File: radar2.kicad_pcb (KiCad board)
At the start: 4 copper layers, 127 parts, among them IC1 BQ25713RSNR, IC2 TPS54540DDA, IC3 LP5907QMFX-3.0Q1, IC5 LP5907QMFX-3.0Q1, IC6 DW3220TR13, J1 GSB1C4621DS1HR, J2 M20-8770546 (for SWD), J3 M20-9730446_DISPLAY_POWER, J4 JST-XH, J5 M20-9990646_PI, J6 SMA_CONNECTOR, J7 SMA_CONNECTOR, Q1 CSD17308Q3, Q2 CSD17308Q3, Q3 CSD17308Q3, Q4 CSD17308Q3, Q5 CSD25404Q3, SW1 09.03290.01, SW2 SWT0220-016016GSA, U1 STM32H725ZETx, Y1 ECS-384-CDX-2482

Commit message: starting routing
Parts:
- moved SW1 94.0 mm to (113.6, 111.5), turned to 90 degrees
- moved J2 68.2 mm to (121.2, 65.6), turned to -90 degrees
- moved J4 26.9 mm to (169.3, 112.8)
- moved C1 22.0 mm to (155.5, 102.5)
- moved C13 22.0 mm to (117.8, 89.0)
- moved C14 22.0 mm to (122.0, 89.0)
- moved C16 22.0 mm to (115.8, 89.0)
- moved C19 22.0 mm to (133.9, 96.9)
- moved C20 22.0 mm to (137.8, 95.8)
- moved C21 22.0 mm to (142.4, 90.9)
- moved C25 22.0 mm to (182.4, 88.4)
- moved C26 22.0 mm to (179.9, 88.4)
- moved C28 22.0 mm to (174.9, 88.4)
- moved C29 22.0 mm to (172.4, 88.4)
- moved C3 22.0 mm to (160.4, 93.8)
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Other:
- board outline added: 127.2 x 59.1 mm

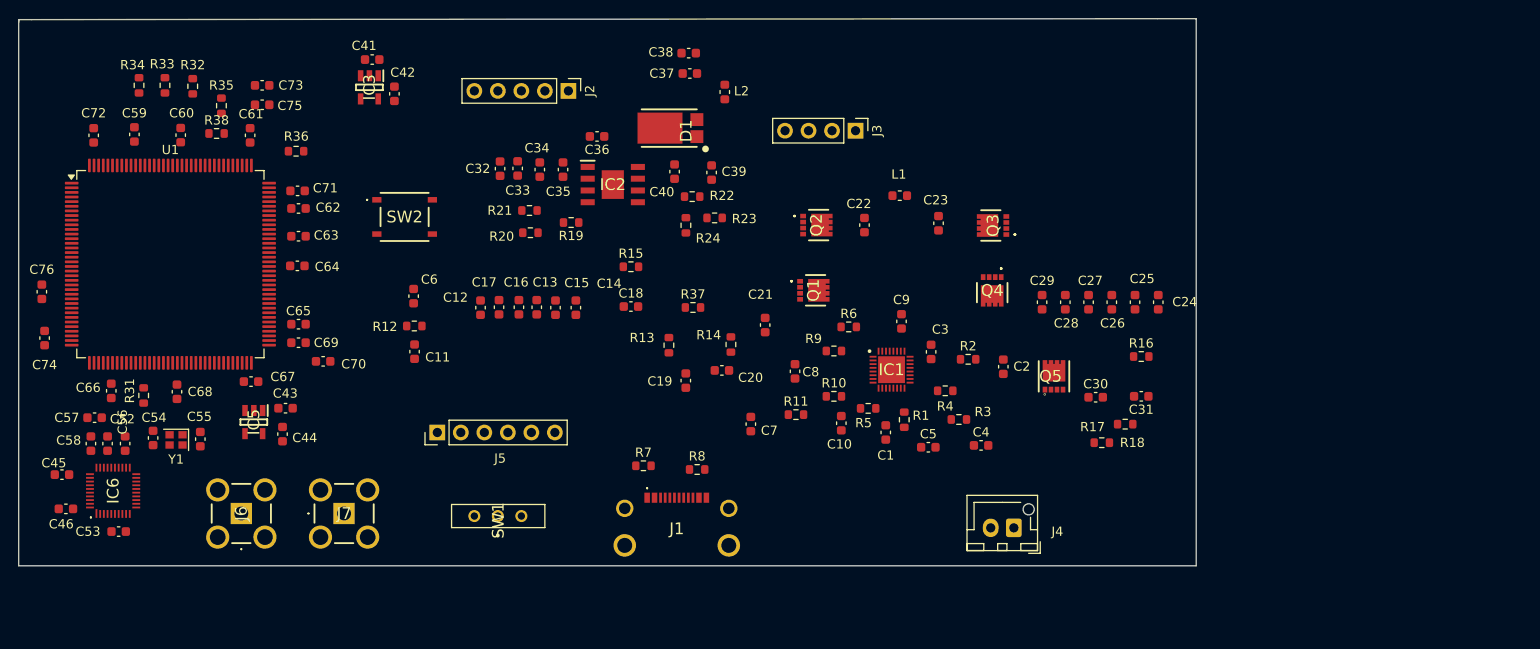
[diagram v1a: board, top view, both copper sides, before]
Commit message: routing on rf ic DW3220
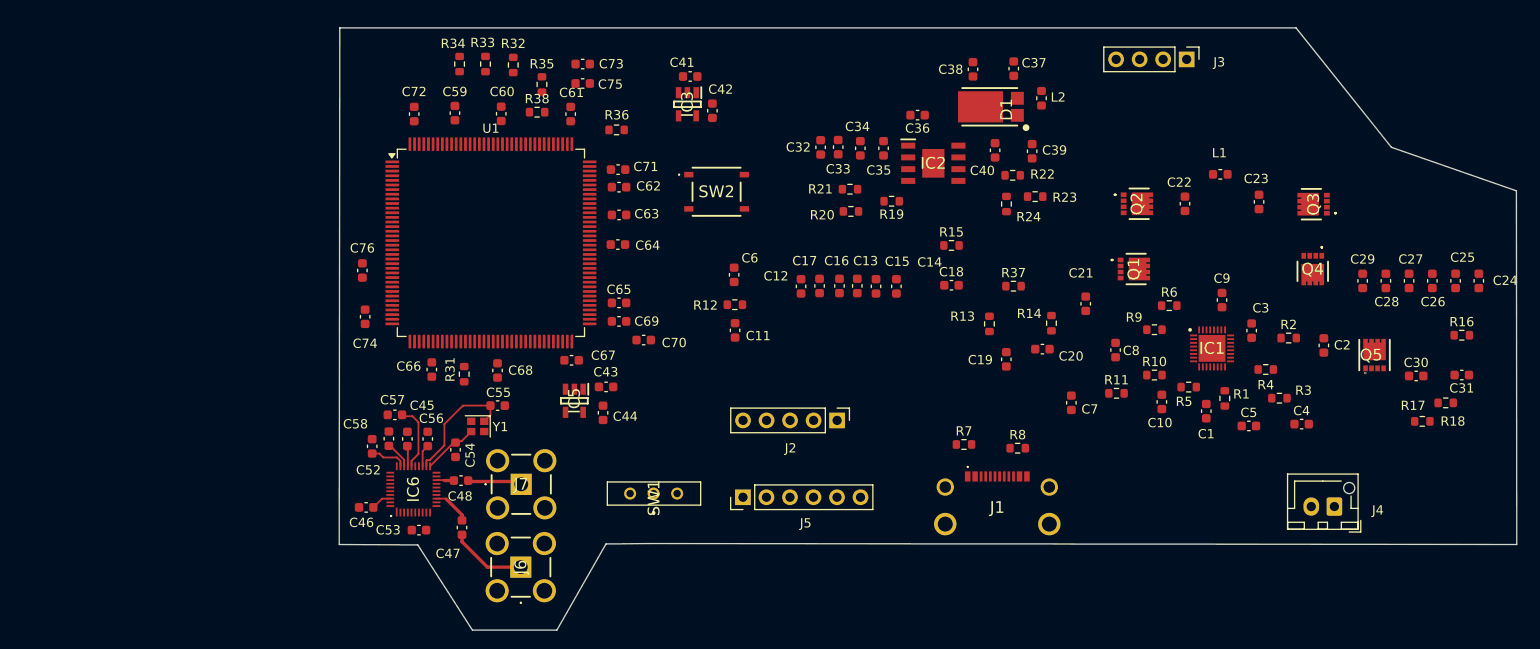
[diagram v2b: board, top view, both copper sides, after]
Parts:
- added C47: 2.0pF, Capacitor_SMD:C_0603_1608Metric, F.Cu at (109.7, 112.8)
- added C48: 2.0pF, Capacitor_SMD:C_0603_1608Metric, F.Cu at (109.6, 107.7)
- moved J2 45.9 mm to (150.2, 101.2)
- moved C45 37.5 mm to (103.8, 103.2), turned to -90 degrees
- moved J3 36.6 mm to (188.0, 62.2)
- moved C37 35.0 mm to (169.3, 63.2), turned to -90 degrees
- moved C15 34.7 mm to (154.4, 86.7)
- moved C34 34.7 mm to (152.7, 71.8)
- moved C36 34.7 mm to (158.9, 68.2)
- moved R12 34.7 mm to (139.2, 88.7)
- moved C1 34.7 mm to (190.1, 100.2)
- moved C10 34.7 mm to (185.3, 99.2)
- moved C13 34.7 mm to (152.4, 86.7)
- moved C14 34.7 mm to (156.6, 86.7)
- moved C16 34.7 mm to (150.5, 86.7)
- moved C19 34.7 mm to (168.5, 94.6)
- moved C2 34.7 mm to (202.8, 93.1)
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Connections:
- J6 pad 1: GND -> Net-(C47-Pad2)
- J6 pad 5: DW_RF2 -> GND
- J7 pad 1: GND -> Net-(C48-Pad2)
- J7 pad 5: DW_RF1 -> GND
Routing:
- net 3V3_RADAR: track 0.00 -> 16.3 mm
- net DW_XTO: track 0.00 -> 13.3 mm
- net Net-(C47-Pad2): track 0.00 -> 8.24 mm
- net DW_XTI: track 0.00 -> 6.00 mm
- net Net-(C48-Pad2): track 0.00 -> 5.89 mm
- net DW_RF2: track 0.00 -> 4.07 mm
- net GND: track 0.00 -> 3.03 mm
- net Net-(IC6-VIO_D): track 0.00 -> 2.22 mm
- net Net-(IC6-VTX_D): track 0.00 -> 2.05 mm
- net DW_RF1: track 0.00 -> 1.90 mm
- added copper zone on In1.Cu, net GND
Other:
- board size 127.2 x 59.1 mm -> 127.2 x 65 mm

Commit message: changing sizes of caps from 06 to 04, also using vias on DW spi interfact to stm32
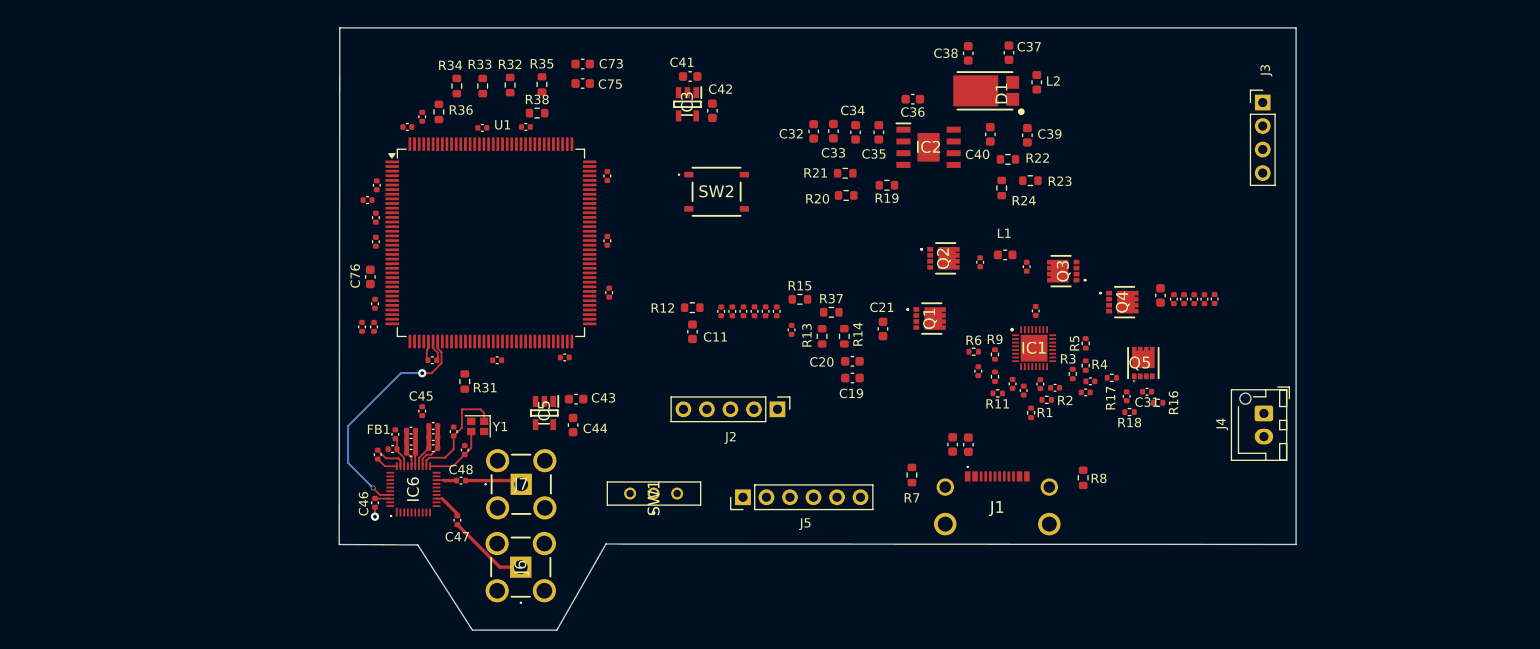
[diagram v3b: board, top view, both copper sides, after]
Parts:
- added C49: 0.1uF, Capacitor_SMD:C_0402_1005Metric, F.Cu at (106.6, 104.2)
- added C50: 4.7nF, Capacitor_SMD:C_0402_1005Metric, F.Cu at (106.6, 103.0)
- added C51: 10uF, Capacitor_SMD:C_0402_1005Metric, F.Cu at (104.2, 102.3)
- added C77: 0.1uF, Capacitor_SMD:C_0402_1005Metric, F.Cu at (100.4, 81.9)
- added C78: 0.1uF, Capacitor_SMD:C_0402_1005Metric, F.Cu at (103.8, 69.5)
- added FB1: 33, Capacitor_SMD:C_0402_1005Metric, F.Cu at (102.5, 102.7)
- C1, C10, C12, C13, C14, C15, C16, C17, C18, C2, C22, C23, C24, C25, C26, C27, C28, C3, C30, C31, C4, C45, C46, C47, C48, C5, C54, C55, C59, C60, C61, C62, C63, C64, C65, C66, C67, C68, C69, C70, C71, C72, C8, C9: footprint Capacitor_SMD:C_0603_1608Metric -> Capacitor_SMD:C_0402_1005Metric
- C52, C58: value 47uF -> 0.1uF; footprint Capacitor_SMD:C_0603_1608Metric -> Capacitor_SMD:C_0402_1005Metric
- C53: value 1uF -> 4.7nF; footprint Capacitor_SMD:C_0603_1608Metric -> Capacitor_SMD:C_0402_1005Metric
- C56: value 47uF -> 4.7nF; footprint Capacitor_SMD:C_0603_1608Metric -> Capacitor_SMD:C_0402_1005Metric
- C57: value 47uF -> 10uF; footprint Capacitor_SMD:C_0603_1608Metric -> Capacitor_SMD:C_0402_1005Metric
- C74: value 4.7uF -> 0.1uF; footprint Capacitor_SMD:C_0603_1608Metric -> Capacitor_SMD:C_0402_1005Metric
- R1, R10, R11, R16, R17, R18, R2, R3, R4, R5, R6, R9: footprint Resistor_SMD:R_0603_1608Metric -> Resistor_SMD:R_0402_1005Metric
- moved R17 36.2 mm to (179.9, 96.6), turned to 0 degrees
- moved C31 34.0 mm to (183.7, 98.1)
- moved R16 33.6 mm to (184.9, 99.3)
- moved R18 31.6 mm to (181.8, 100.3)
- moved C30 31.4 mm to (181.5, 98.6), turned to 90 degrees
- moved C70 30.5 mm to (98.9, 91.1), turned to 90 degrees
- moved C6 29.9 mm to (162.7, 103.8), turned to 90 degrees
- moved C2 29.4 mm to (173.8, 97.7), turned to 0 degrees
- moved C24 28.6 mm to (191.0, 88.1), turned to 90 degrees
- moved Q3 28.0 mm to (174.6, 85.1)
- moved C71 27.3 mm to (99.5, 77.4), turned to 0 degrees
- moved C25 27.2 mm to (189.9, 88.1), turned to 90 degrees
- moved R2 27.0 mm to (172.9, 99.0)
- moved C69 26.5 mm to (100.2, 91.1), turned to 90 degrees
- moved C62 26.5 mm to (100.4, 79.3), turned to 90 degrees
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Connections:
- C32 pad 2: Net-(IC2-VIN) -> /pmics/VSYS
- C33 pad 2: Net-(IC2-VIN) -> /pmics/VSYS
- C34 pad 2: Net-(IC2-VIN) -> /pmics/VSYS
- C35 pad 2: Net-(IC2-VIN) -> /pmics/VSYS
- C53 pad 1: 3V3_RADAR -> DW_VDD2A
- IC2 pad 2: Net-(IC2-VIN) -> /pmics/VSYS
- IC6 pad 28: 3V3_RADAR -> DW_VDD2A
- R20 pad 1: Net-(IC2-VIN) -> /pmics/VSYS
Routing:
- net DW_SPICSN: track 0.00 -> 25.4 mm, vias 0 -> 2
- net GND: track 3.03 -> 17.2 mm, vias 0 -> 1
- net 3V3_RADAR: track 16.3 -> 12.9 mm
- net DW_VDD2A: track 0.00 -> 3.36 mm
- net 3V3_MCU: track 0.00 -> 2.28 mm
- net Net-(IC6-VTX_D): track 2.05 -> 0.00 mm
- net DW_XTO: track 13.3 -> 12.2 mm
- net DW_XTI: track 6.00 -> 7.05 mm
- net DW_RF2: track 4.07 -> 3.13 mm
- net Net-(IC6-VIO_D): track 2.22 -> 1.66 mm
- net Net-(C47-Pad2): track 8.24 -> 8.75 mm
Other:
- board size 127.2 x 65 mm -> 103.4 x 65 mm

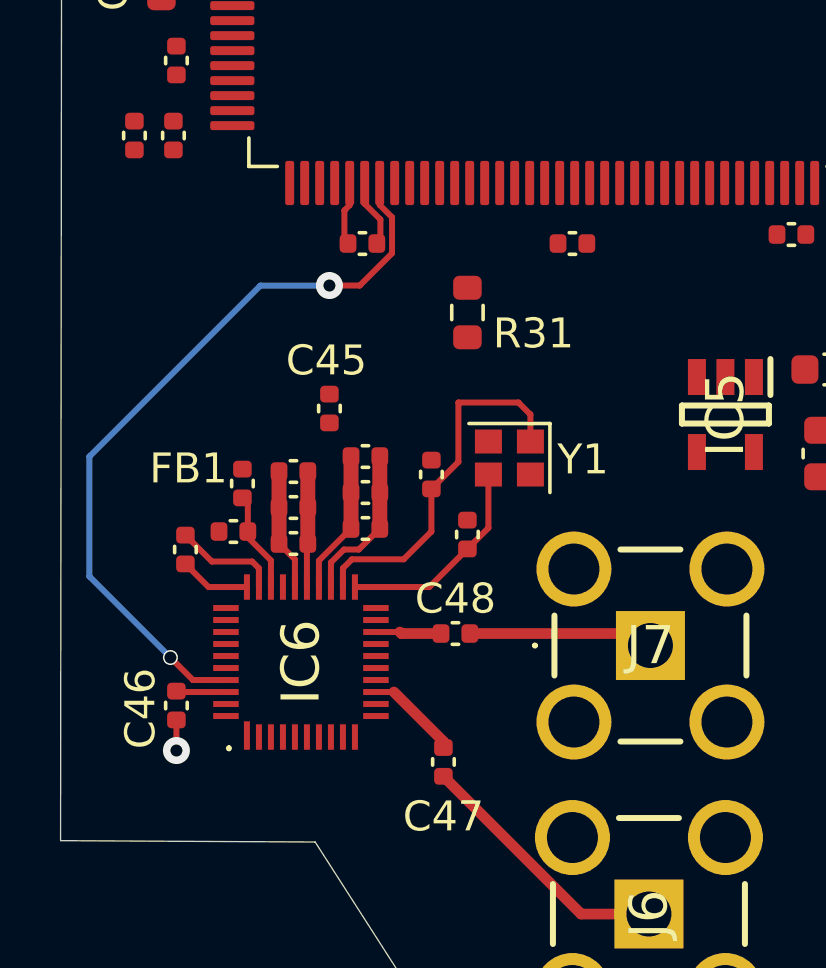
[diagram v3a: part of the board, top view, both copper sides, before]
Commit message: more routing for rf ic, adding readme and picture
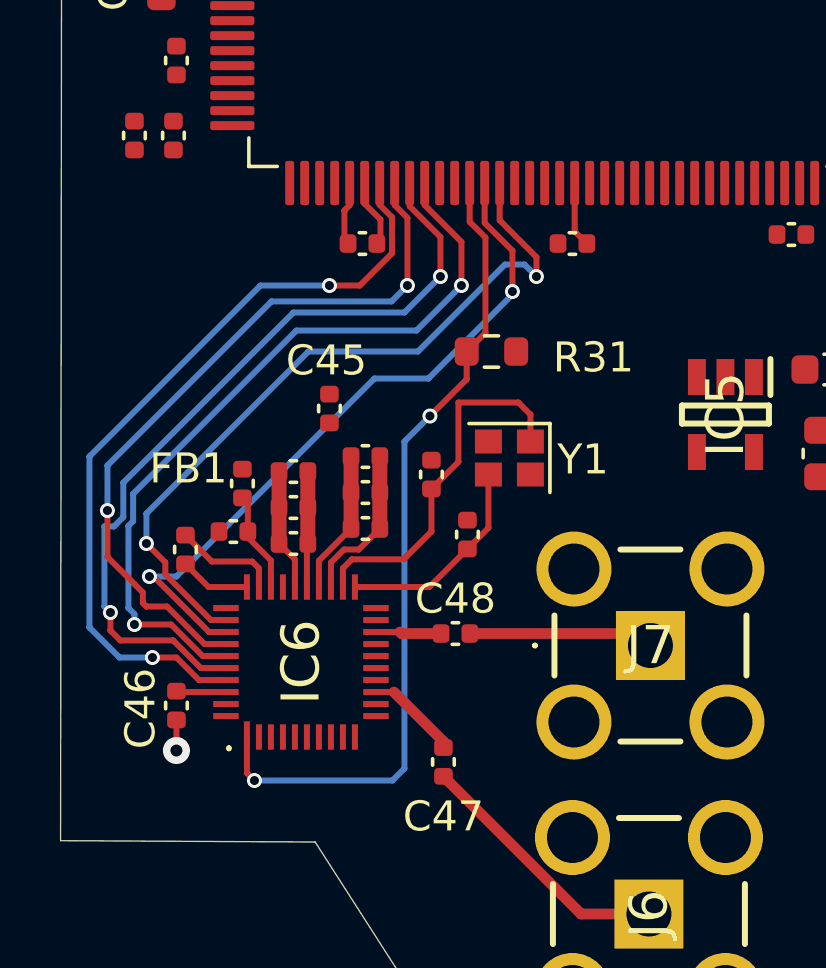
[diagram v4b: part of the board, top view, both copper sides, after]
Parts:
- moved R31 1.53 mm to (110.8, 98.3), turned to 0 degrees
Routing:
- net DW_IRQ: track 0.00 -> 27.6 mm, vias 0 -> 2
- net DW_SPIMISO: track 0.00 -> 26.8 mm, vias 0 -> 2
- net DW_SPIMOSI: track 0.00 -> 25.7 mm, vias 0 -> 2
- net DW_WKUP: track 0.00 -> 25.2 mm, vias 0 -> 2
- net DW_SPICLK: track 0.00 -> 24.5 mm, vias 0 -> 2
- net DW_nRST: track 0.00 -> 23.4 mm, vias 0 -> 2
- net 3V3_MCU: track 2.28 -> 4.47 mm
- net DW_SPICSN: track 25.4 -> 26.4 mm

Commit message: working on routing the 4 switch mosfet arch
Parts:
- moved C45 2.92 mm to (102.5, 100.5), turned to 0 degrees
- moved C51 0.58 mm to (104.5, 101.8)
- moved C52 0.58 mm to (104.5, 103.0)
- moved C56 0.58 mm to (104.5, 104.2)
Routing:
- net VBUS: track 0.00 -> 15.2 mm
- net GND: track 17.2 -> 32.2 mm, vias 1 -> 5
- net Net-(J1-CC1): track 0.00 -> 11.3 mm
- net Net-(J1-CC2): track 0.00 -> 9.92 mm
- net 3V3_MCU: track 4.47 -> 10.5 mm
- net Net-(IC6-VTX_D): track 0.00 -> 6.01 mm
- net DW_nRST: track 23.4 -> 24.0 mm

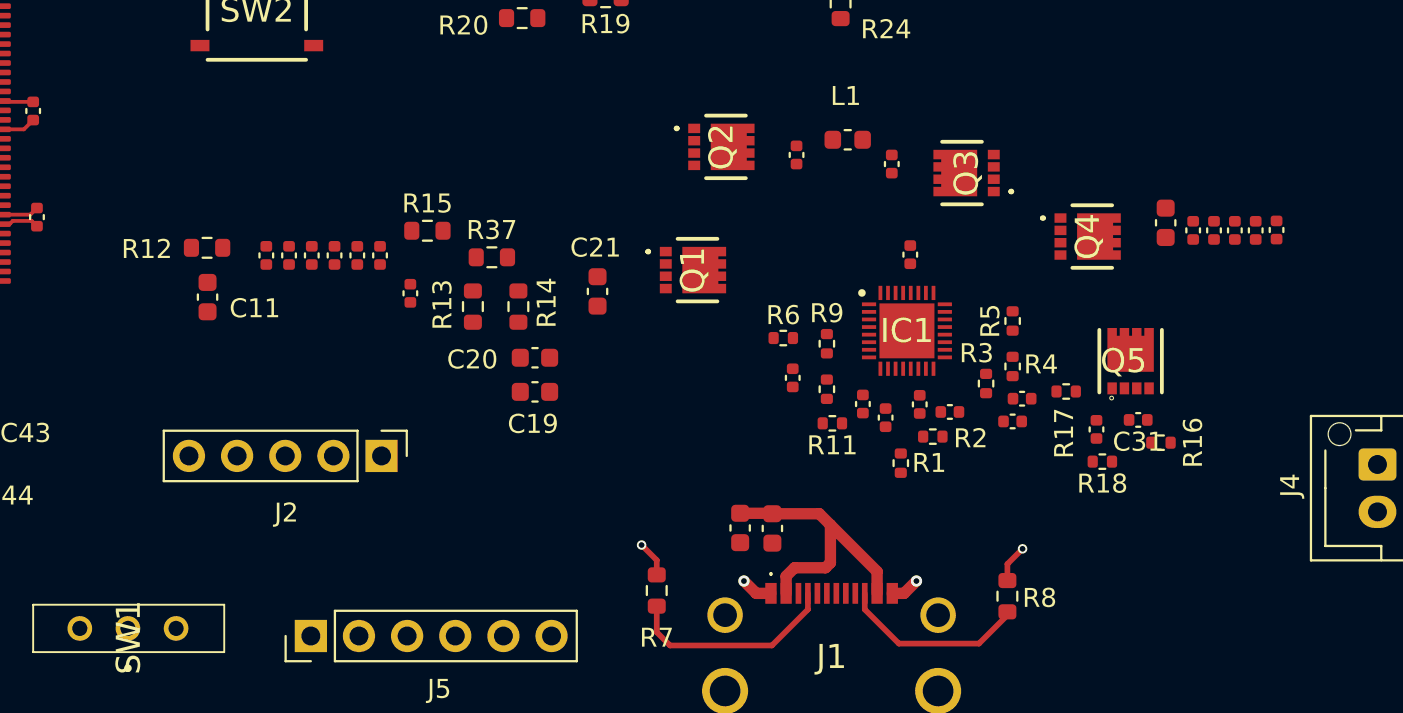
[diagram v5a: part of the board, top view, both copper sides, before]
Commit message: routing rails and BQ 4 switch mosfets
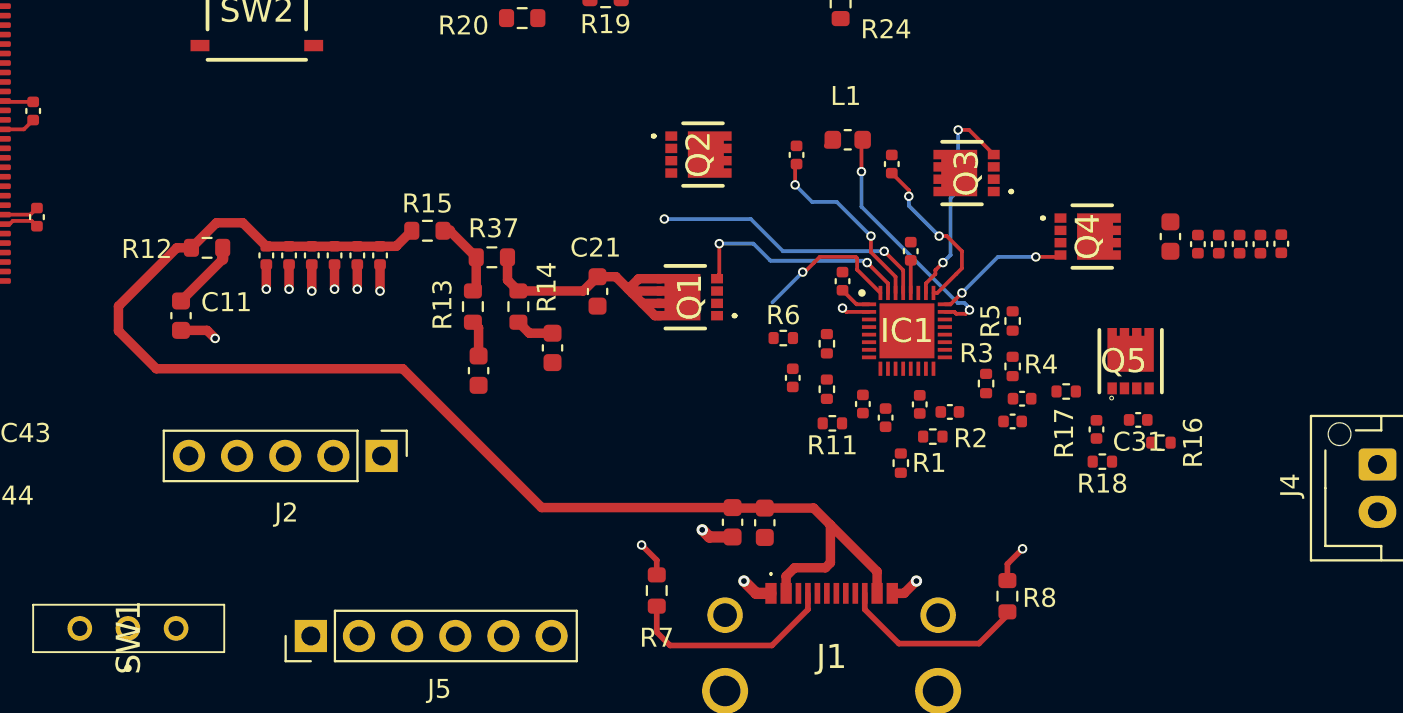
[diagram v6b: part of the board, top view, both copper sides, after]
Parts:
- moved C18 22.8 mm to (168.1, 90.8), turned to -90 degrees
- moved C19 3.18 mm to (148.9, 95.5), turned to 90 degrees
- moved C11 1.71 mm to (133.2, 92.6)
- moved Q1 1.44 mm to (160.0, 91.6), turned to 90 degrees
- moved Q2 1.28 mm to (160.5, 84.1)
- moved C20 1.06 mm to (152.8, 94.3), turned to 90 degrees
- moved C24 0.77 mm to (191.2, 88.8)
- moved C25 0.77 mm to (190.2, 88.8)
- moved C26 0.77 mm to (189.1, 88.8)
- moved C27 0.77 mm to (187.9, 88.8)
- moved C28 0.77 mm to (186.8, 88.8)
- moved C29 0.77 mm to (185.4, 88.4)
- moved C7 0.50 mm to (164.0, 103.5)
- moved C6 0.50 mm to (162.3, 103.5)
- moved C9 0.18 mm to (171.7, 89.2)
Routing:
- net VBUS: track 15.2 -> 77.3 mm
- net Net-(Q1-D_1): track 0.00 -> 15.1 mm
- net /pmics/LODRV1: track 0.00 -> 14.9 mm, vias 0 -> 2
- net /pmics/SW2: track 0.00 -> 13.0 mm, vias 0 -> 2
- net /pmics/HIDRV1: track 0.00 -> 12.2 mm, vias 0 -> 2
- net GND: track 32.2 -> 43.9 mm, vias 5 -> 13
- net /pmics/LODRV2: track 0.00 -> 11.7 mm, vias 0 -> 2
- net /pmics/BTST1: track 0.00 -> 9.79 mm, vias 0 -> 2
- net /pmics/BTST2: track 0.00 -> 8.83 mm, vias 0 -> 2
- net /pmics/SW1: track 0.00 -> 8.36 mm, vias 0 -> 1
- net /pmics/HIDRV2: track 0.00 -> 7.18 mm, vias 0 -> 2
- net Net-(C11-Pad1): track 0.00 -> 3.72 mm
- net /pmics/ACN: track 0.00 -> 3.52 mm, vias 0 -> 1
- net /pmics/ACP: track 0.00 -> 1.90 mm
- net /pmics/REGN: track 0.00 -> 1.55 mm
